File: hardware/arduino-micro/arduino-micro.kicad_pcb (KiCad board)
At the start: 2 copper layers, 80 x 44.5 mm, 17 parts, among them J1 PJ-028-SMT-TR, M1 Fan_4pin, SW1 Rotary_Encoder, U1 TM1637, U2 CA56-12CGKWA

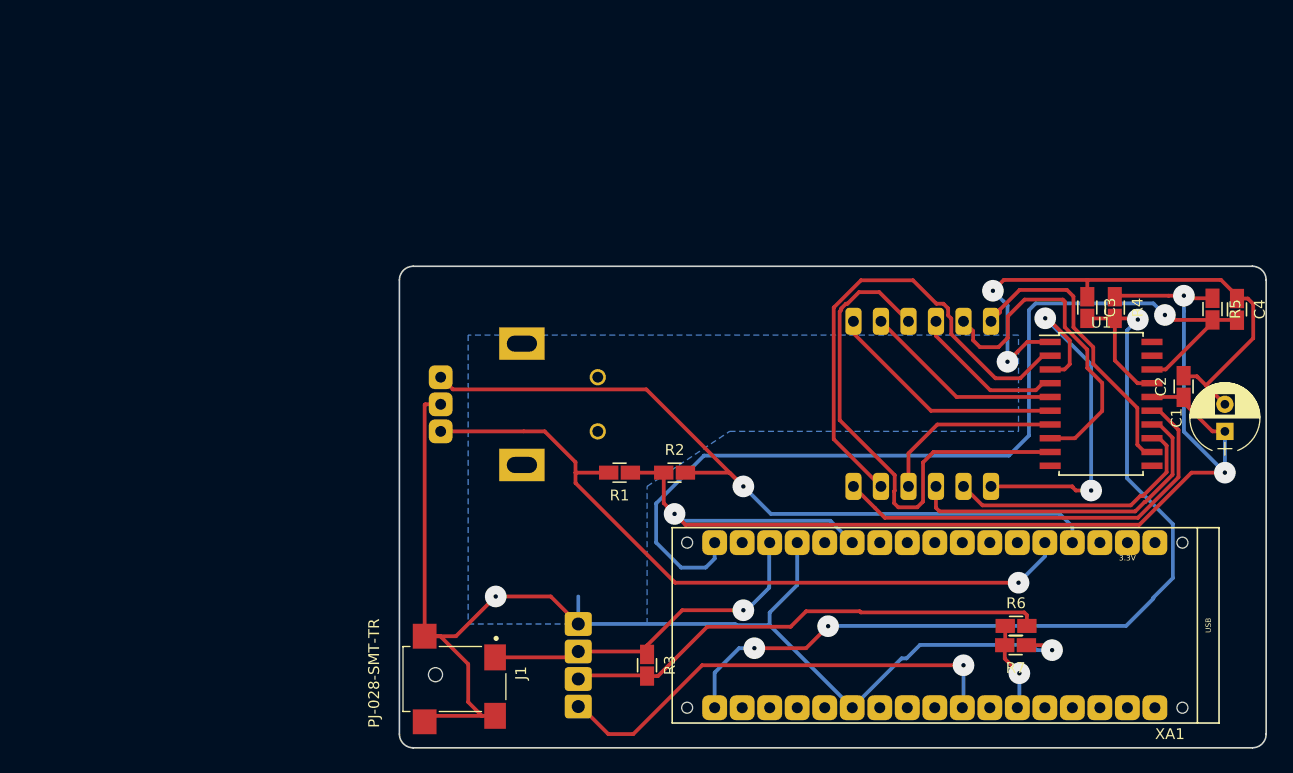
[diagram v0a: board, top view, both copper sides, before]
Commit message: New Prototype Board (#3)
* checkpoint before removing board

* redesign board, additional buttons/i2c header

* fix 5v for i2c header

* voltage regulator footprint

* board updates for prototype
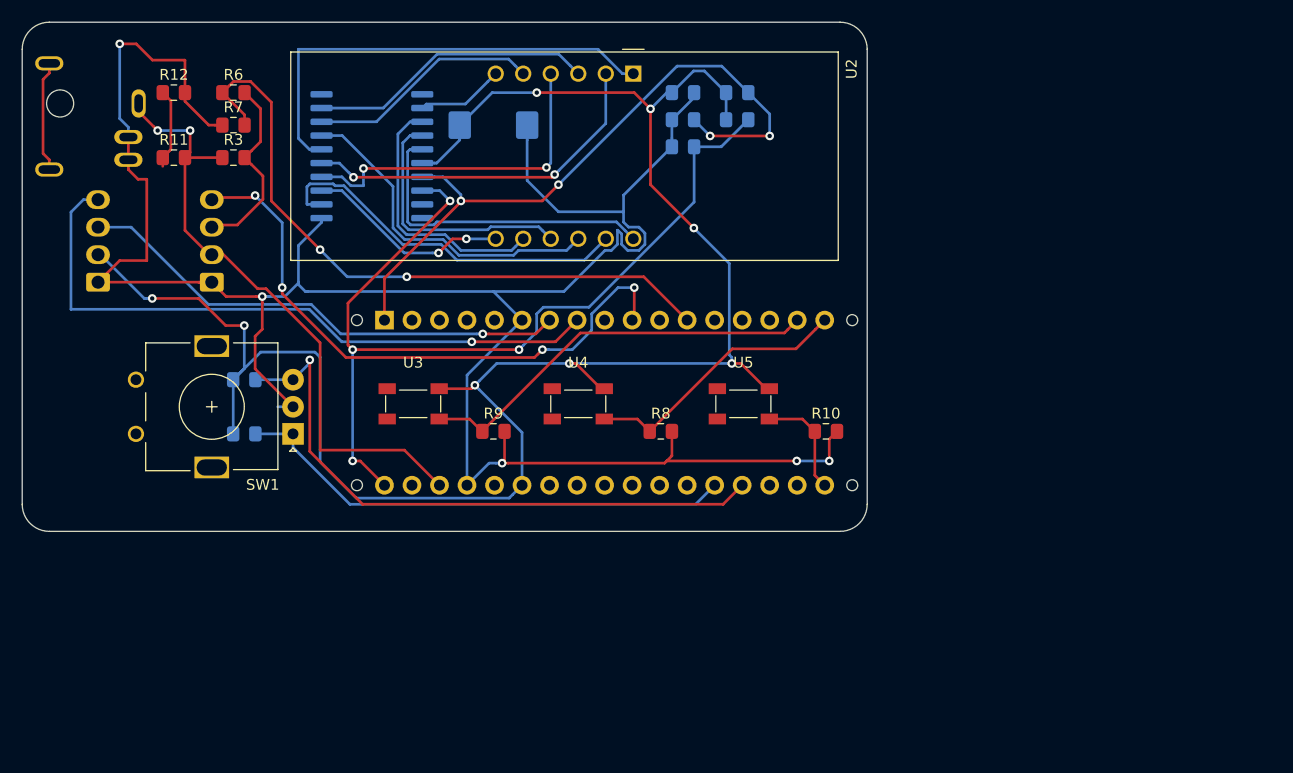
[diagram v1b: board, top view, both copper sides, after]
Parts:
- added J2: i2c_header, Connector_Molex:Molex_KK-254_AE-6410-04A_1x04_P2.54mm_Vertical, B.Cu at (119.5, 114.5)
- added R10: 10k, Resistor_SMD:R_0805_2012Metric_Pad1.15x1.40mm_HandSolder, F.Cu at (186.7, 128.3)
- added R11: 14k, Resistor_SMD:R_0805_2012Metric_Pad1.15x1.40mm_HandSolder, F.Cu at (126.5, 103.0)
- added R12: 10k, Resistor_SMD:R_0805_2012Metric_Pad1.15x1.40mm_HandSolder, F.Cu at (126.5, 97.0)
- added R8: 10k, Resistor_SMD:R_0805_2012Metric_Pad1.15x1.40mm_HandSolder, F.Cu at (171.4, 128.3)
- added R9: 10k, Resistor_SMD:R_0805_2012Metric_Pad1.15x1.40mm_HandSolder, F.Cu at (156.0, 128.3)
- added U3: BUTTON_1, squeeze-misc:PTS525_SM15_SMTR2_LFS, F.Cu at (148.6, 125.7)
- added U4: BUTTON_2, squeeze-misc:PTS525_SM15_SMTR2_LFS, F.Cu at (163.8, 125.7)
- added U5: BUTTON_3, squeeze-misc:PTS525_SM15_SMTR2_LFS, F.Cu at (179.1, 125.7)
- C1: footprint Capacitors_THT:CP_Radial_D6.3mm_P2.50mm -> Capacitor_Tantalum_SMD:CP_EIA-7343-31_Kemet-D; moved to B.Cu
- C2, C3, C4, R1, R2, R4, R5: footprint coddingtonbear:0805_Milling -> Resistor_SMD:R_0805_2012Metric_Pad1.15x1.40mm_HandSolder; moved to B.Cu
- J1: value PJ-028-SMT-TR -> PJ-083H; footprint PJ-028-SMT-TR:CUI_PJ-028-SMT-TR -> squeeze-misc:CUI_PJ-083H; moved to B.Cu
- R3, R6, R7: footprint coddingtonbear:0805_Milling -> Resistor_SMD:R_0805_2012Metric_Pad1.15x1.40mm_HandSolder
- SW1, U2: moved to F.Cu
- U1, XA1: moved to B.Cu
- moved R6 87.4 mm to (132.0, 97.0)
- moved R7 86.7 mm to (132.0, 100.0), turned to 0 degrees
- moved C1 73.2 mm to (156.0, 100.0), turned to 0 degrees
- moved U1 71.1 mm to (144.8, 102.9)
- moved J1 66.7 mm to (112.0, 98.0), turned to 0 degrees
- moved R3 60.4 mm to (132.0, 103.0), turned to 0 degrees
- moved C2 53.6 mm to (173.5, 97.0), turned to 0 degrees
- moved C4 53.3 mm to (173.5, 102.0), turned to 0 degrees
- moved R5 47.2 mm to (178.5, 99.5), turned to 0 degrees
- moved M1 46.3 mm to (130.0, 114.5), turned to 90 degrees
- moved C3 41.2 mm to (173.5, 99.5), turned to 0 degrees
- moved R2 40.6 mm to (133.0, 123.5)
- moved R4 40.1 mm to (178.5, 97.0), turned to 0 degrees
- moved R1 34.8 mm to (133.0, 128.5), turned to 0 degrees
- moved U2 30.6 mm to (168.9, 95.2)
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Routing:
- net Net-(J2-Pad4): track 0.00 -> 60.7 mm, vias 0 -> 1
- net /5V: track 118.3 -> 177.3 mm, vias 3 -> 8
- net Net-(R6-Pad1): track 8.20 -> 61.6 mm, vias 1 -> 2
- net Net-(J2-Pad3): track 0.00 -> 46.3 mm, vias 0 -> 1
- net GND: track 173.1 -> 217.5 mm, vias 4 -> 5
- net Net-(R9-Pad1): track 0.00 -> 37.8 mm
- net Net-(M1-Pad3): track 45.2 -> 17.9 mm
- net +12V: track 32.9 -> 59.2 mm, vias 1 -> 2
- net Net-(R8-Pad1): track 0.00 -> 25.1 mm
- net /7S_IO: track 88.1 -> 63.9 mm, vias 3 -> 4
- net Net-(R1-Pad2): track 68.1 -> 46.5 mm, vias 1 -> 0
- net Net-(U1-Pad6): track 22.2 -> 42.6 mm
- net Net-(U1-Pad9): track 46.9 -> 26.5 mm
- net Net-(U1-Pad12): track 27.0 -> 8.10 mm
- net Net-(U1-Pad4): track 14.2 -> 31.5 mm, vias 0 -> 2
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- removed copper zone on B.Cu, net GND
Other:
- board size 80 x 44.5 mm -> 78 x 47 mm
- net class Default: trace_width 0.35 -> 0.25; via_dia 2 -> 0.8
- rule pad_to_mask_clearance: 0.051 -> 0.2032
